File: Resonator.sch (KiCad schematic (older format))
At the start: 29 parts, among them J1 Conn_01x04_Male, SW1 Rotary_Encoder_Switch, SW2 SW_Push, U1 STM32H750VBTx, U2 AT25xxx, U3 IPS240x240, Y1 ABM8G-25.000MHZ-18-D2Y-T

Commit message: Re-annotation.
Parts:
- renumbered R4 to R1, R5 to R2, R6 to R3, R1 to R4, R7 to R5, R2 to R6, R3 to R7, SW2 to SW1, SW1 to SW2, U3 to U2, U2 to U3
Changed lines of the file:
@@
 $Descr A3 16535 11693
 encoding utf-8
-Sheet 1 6
+Sheet 1 11
 Title "Resonator"
 Date "2021-11-21"
@@
 Connection ~ 7650 2750
 $Comp
-L power:+3.3V #PWR013
+L power:+3.3V #PWR012
 U 1 1 61D958D9
 P 7650 2750
-F 0 "#PWR013" H 7650 2600 50  0001 C CNN
+F 0 "#PWR012" H 7650 2600 50  0001 C CNN
 F 1 "+3.3V" H 7665 2923 50  0000 C CNN
 F 2 "" H 7650 2750 50  0001 C CNN
@@
 $EndComp
 $Comp
-L power:+3.3VA #PWR016
+L power:+3.3VA #PWR015
 U 1 1 61D96DEA
 P 8150 2750
-F 0 "#PWR016" H 8150 2600 50  0001 C CNN
+F 0 "#PWR015" H 8150 2600 50  0001 C CNN
 F 1 "+3.3VA" H 8165 2923 50  0000 C CNN
 F 2 "" H 8150 2750 50  0001 C CNN
@@
 $EndComp
 $Comp
-L power:GND #PWR012
+L power:GND #PWR011
 U 1 1 61D9B5CB
 P 7550 8250
-F 0 "#PWR012" H 7550 8000 50  0001 C CNN
+F 0 "#PWR011" H 7550 8000 50  0001 C CNN
 F 1 "GND" H 7555 8077 50  0000 C CNN
 F 2 "" H 7550 8250 50  0001 C CNN
@@
 	6950 3550 6950 3450
 $Comp
-L power:GND #PWR010
+L power:GND #PWR09
 U 1 1 61DA19D2
 P 6050 3800
-F 0 "#PWR010" H 6050 3550 50  0001 C CNN
+F 0 "#PWR09" H 6050 3550 50  0001 C CNN
 F 1 "GND" H 6055 3627 50  0000 C CNN
 F 2 "" H 6050 3800 50  0001 C CNN
@@
 Connection ~ 6050 3800
 $Comp
-L power:+3V3 #PWR04
+L power:+3V3 #PWR03
 U 1 1 61DAD533
 P 4050 10300
-F 0 "#PWR04" H 4050 10150 50  0001 C CNN
+F 0 "#PWR03" H 4050 10150 50  0001 C CNN
 F 1 "+3V3" H 4065 10473 50  0000 C CNN
 F 2 "" H 4050 10300 50  0001 C CNN
@@
 	4050 10300 4200 10300
 $Comp
-L power:GND #PWR05
+L power:GND #PWR04
 U 1 1 61DAD53E
 P 4050 10600
-F 0 "#PWR05" H 4050 10350 50  0001 C CNN
+F 0 "#PWR04" H 4050 10350 50  0001 C CNN
 F 1 "GND" H 4055 10427 50  0000 C CNN
 F 2 "" H 4050 10600 50  0001 C CNN
@@
 $EndComp
 $Comp
-L Device:R R4
+L Device:R R1
 U 1 1 61DB7AD0
 P 5750 3050
-F 0 "R4" V 5543 3050 50  0000 C CNN
+F 0 "R1" V 5543 3050 50  0000 C CNN
 F 1 "UNPOPULATED" V 5634 3050 50  0000 C CNN
 F 2 "Resistor_SMD:R_0603_1608Metric" V 5680 3050 50  0001 C CNN
@@
 $EndComp
 $Comp
-L Switch:SW_Push SW2
+L Switch:SW_Push SW1
 U 1 1 61DBD527
 P 6750 3050
-F 0 "SW2" H 6750 3335 50  0000 C CNN
+F 0 "SW1" H 6750 3335 50  0000 C CNN
 F 1 "SW_Push" H 6750 3244 50  0000 C CNN
 F 2 "Button_Switch_THT:SW_PUSH_6mm" H 6750 3250 50  0001 C CNN
@@
 	6950 2600 6900 2600
 $Comp
-L power:GND #PWR011
+L power:GND #PWR010
 U 1 1 61DC8FB1
 P 6300 2750
-F 0 "#PWR011" H 6300 2500 50  0001 C CNN
+F 0 "#PWR010" H 6300 2500 50  0001 C CNN
 F 1 "GND" H 6305 2577 50  0000 C CNN
 F 2 "" H 6300 2750 50  0001 C CNN
@@
 	5700 4700 5700 4450
 $Comp
-L power:GND #PWR07
+L power:GND #PWR06
 U 1 1 61E01E16
 P 5700 5050
-F 0 "#PWR07" H 5700 4800 50  0001 C CNN
+F 0 "#PWR06" H 5700 4800 50  0001 C CNN
 F 1 "GND" H 5705 4877 50  0000 C CNN
 F 2 "" H 5700 5050 50  0001 C CNN
@@
 	7750 10300 7900 10300
 $Comp
-L power:GND #PWR015
+L power:GND #PWR014
 U 1 1 61E8662A
 P 7750 10600
-F 0 "#PWR015" H 7750 10350 50  0001 C CNN
+F 0 "#PWR014" H 7750 10350 50  0001 C CNN
 F 1 "GND" H 7755 10427 50  0000 C CNN
 F 2 "" H 7750 10600 50  0001 C CNN
@@
 	7750 10600 7900 10600
 $Comp
-L power:+3.3VA #PWR014
+L power:+3.3VA #PWR013
 U 1 1 61E8B8BA
 P 7750 10300
-F 0 "#PWR014" H 7750 10150 50  0001 C CNN
+F 0 "#PWR013" H 7750 10150 50  0001 C CNN
 F 1 "+3.3VA" H 7765 10473 50  0000 C CNN
 F 2 "" H 7750 10300 50  0001 C CNN
@@
 	7900 10600 8300 10600
 $Comp
-L Device:R R5
+L Device:R R2
 U 1 1 61ADEFE2
 P 5750 3450
-F 0 "R5" V 5543 3450 50  0000 C CNN
+F 0 "R2" V 5543 3450 50  0000 C CNN
 F 1 "10k" V 5634 3450 50  0000 C CNN
 F 2 "Resistor_SMD:R_0603_1608Metric" V 5680 3450 50  0001 C CNN
@@
 	6100 4800 6100 4950
 $Comp
-L Device:R R6
+L Device:R R3
 U 1 1 61AE0744
 P 6250 4950
-F 0 "R6" V 6043 4950 50  0000 C CNN
+F 0 "R3" V 6043 4950 50  0000 C CNN
 F 1 "470" V 6134 4950 50  0000 C CNN
 F 2 "Resistor_SMD:R_0603_1608Metric" V 6180 4950 50  0001 C CNN
@@
 	5750 3250 5750 3200
 $Comp
-L power:GND #PWR09
+L power:GND #PWR08
 U 1 1 61AF8BC1
 P 5750 3600
-F 0 "#PWR09" H 5750 3350 50  0001 C CNN
+F 0 "#PWR08" H 5750 3350 50  0001 C CNN
 F 1 "GND" H 5755 3427 50  0000 C CNN
 F 2 "" H 5750 3600 50  0001 C CNN
@@
 $EndComp
 $Comp
-L power:+3.3V #PWR08
+L power:+3.3V #PWR07
 U 1 1 61AF9828
 P 5750 2900
-F 0 "#PWR08" H 5750 2750 50  0001 C CNN
+F 0 "#PWR07" H 5750 2750 50  0001 C CNN
 F 1 "+3.3V" H 5765 3073 50  0000 C CNN
 F 2 "" H 5750 2900 50  0001 C CNN
@@
 P 13200 6950
 AR Path="/5DD41DD6/61DD28C6" Ref="U?"  Part="1"
-AR Path="/61DD28C6" Ref="U2"  Part="1"
+AR Path="/61DD28C6" Ref="U3"  Part="1"
 AR Path="/61DB1EC2/61DD28C6" Ref="U?"  Part="1"
-F 0 "U2" H 13200 7431 50  0000 C CNN
+F 0 "U3" H 13200 7431 50  0000 C CNN
 F 1 "AT25xxx" H 13200 7340 50  0000 C CNN
 F 2 "Package_SO:TSSOP-8_4.4x3mm_P0.65mm" H 13200 6950 50  0001 C CNN
@@
 P 13200 7350
 AR Path="/5DD41DD6/61DD28CC" Ref="#PWR?"  Part="1"
-AR Path="/61DD28CC" Ref="#PWR024"  Part="1"
+AR Path="/61DD28CC" Ref="#PWR018"  Part="1"
 AR Path="/61DB1EC2/61DD28CC" Ref="#PWR?"  Part="1"
-F 0 "#PWR024" H 13200 7100 50  0001 C CNN
+F 0 "#PWR018" H 13200 7100 50  0001 C CNN
 F 1 "GND" H 13205 7177 50  0000 C CNN
 F 2 "" H 13200 7350 50  0001 C CNN
@@
 P 13200 6400
 AR Path="/5DD41DD6/61DD28D3" Ref="#PWR?"  Part="1"
-AR Path="/61DD28D3" Ref="#PWR023"  Part="1"
+AR Path="/61DD28D3" Ref="#PWR017"  Part="1"
 AR Path="/61DB1EC2/61DD28D3" Ref="#PWR?"  Part="1"
-F 0 "#PWR023" H 13200 6250 50  0001 C CNN
+F 0 "#PWR017" H 13200 6250 50  0001 C CNN
 F 1 "+3.3V" H 13215 6573 50  0000 C CNN
 F 2 "" H 13200 6400 50  0001 C CNN
@@
 P 13300 3500
 AR Path="/5DD41DD6/61DE3E76" Ref="SW?"  Part="1"
-AR Path="/61DE3E76" Ref="SW1"  Part="1"
+AR Path="/61DE3E76" Ref="SW2"  Part="1"
 AR Path="/61DB1EC2/61DE3E76" Ref="SW?"  Part="1"
-F 0 "SW1" H 13300 3867 50  0000 C CNN
+F 0 "SW2" H 13300 3867 50  0000 C CNN
 F 1 "Rotary_Encoder_Switch" H 13300 3776 50  0000 C CNN
 F 2 "Rotary_Encoder:RotaryEncoder_Alps_EC11E-Switch_Vertical_H20mm" H 13150 3660 50  0001 C CNN
@@
 P 13300 3900
 AR Path="/5DD41DD6/61DE3E7C" Ref="#PWR?"  Part="1"
-AR Path="/61DE3E7C" Ref="#PWR03"  Part="1"
+AR Path="/61DE3E7C" Ref="#PWR019"  Part="1"
 AR Path="/61DB1EC2/61DE3E7C" Ref="#PWR?"  Part="1"
-F 0 "#PWR03" H 13300 3650 50  0001 C CNN
+F 0 "#PWR019" H 13300 3650 50  0001 C CNN
 F 1 "GND" H 13305 3727 50  0000 C CNN
 F 2 "" H 13300 3900 50  0001 C CNN
@@
 P 13750 3050
 AR Path="/61DB1EC2/61DE3E90" Ref="R?"  Part="1"
-AR Path="/61DE3E90" Ref="R3"  Part="1"
-F 0 "R3" H 13820 3096 50  0000 L CNN
+AR Path="/61DE3E90" Ref="R7"  Part="1"
+F 0 "R7" H 13820 3096 50  0000 L CNN
 F 1 "10k" H 13820 3005 50  0000 L CNN
 F 2 "Resistor_SMD:R_0603_1608Metric" V 13680 3050 50  0001 C CNN
@@
 P 12800 3050
 AR Path="/61DB1EC2/61DE3E96" Ref="R?"  Part="1"
-AR Path="/61DE3E96" Ref="R2"  Part="1"
-F 0 "R2" H 12870 3096 50  0000 L CNN
+AR Path="/61DE3E96" Ref="R6"  Part="1"
+F 0 "R6" H 12870 3096 50  0000 L CNN
 F 1 "10k" H 12870 3005 50  0000 L CNN
 F 2 "Resistor_SMD:R_0603_1608Metric" V 12730 3050 50  0001 C CNN
@@
 P 12500 3050
 AR Path="/61DB1EC2/61DE3E9C" Ref="R?"  Part="1"
-AR Path="/61DE3E9C" Ref="R1"  Part="1"
-F 0 "R1" H 12570 3096 50  0000 L CNN
+AR Path="/61DE3E9C" Ref="R4"  Part="1"
+F 0 "R4" H 12570 3096 50  0000 L CNN
 F 1 "10k" H 12570 3005 50  0000 L CNN
 F 2 "Resistor_SMD:R_0603_1608Metric" V 12430 3050 50  0001 C CNN
@@
 P 12500 2750
 AR Path="/61DB1EC2/61DE3EAB" Ref="#PWR?"  Part="1"
-AR Path="/61DE3EAB" Ref="#PWR01"  Part="1"
-F 0 "#PWR01" H 12500 2600 50  0001 C CNN
+AR Path="/61DE3EAB" Ref="#PWR016"  Part="1"
+F 0 "#PWR016" H 12500 2600 50  0001 C CNN
 F 1 "+3.3V" H 12515 2923 50  0000 C CNN
 F 2 "" H 12500 2750 50  0001 C CNN
@@
 P 5550 9350
 AR Path="/5DD41DD6/61DED307" Ref="#PWR?"  Part="1"
-AR Path="/61DED307" Ref="#PWR06"  Part="1"
+AR Path="/61DED307" Ref="#PWR05"  Part="1"
 AR Path="/61DB1EC2/61DED307" Ref="#PWR?"  Part="1"
-F 0 "#PWR06" H 5550 9100 50  0001 C CNN
+F 0 "#PWR05" H 5550 9100 50  0001 C CNN
 F 1 "GND" H 5555 9177 50  0000 C CNN
 F 2 "" H 5550 9350 50  0001 C CNN
@@
 P 12700 5250
 AR Path="/5DD41DD6/61E13169" Ref="R?"  Part="1"
-AR Path="/61E13169" Ref="R7"  Part="1"
+AR Path="/61E13169" Ref="R5"  Part="1"
 AR Path="/61DB1EC2/61E13169" Ref="R?"  Part="1"
-F 0 "R7" V 12493 5250 50  0000 C CNN
+F 0 "R5" V 12493 5250 50  0000 C CNN
 F 1 "1k" V 12584 5250 50  0000 C CNN
 F 2 "Resistor_SMD:R_0603_1608Metric" V 12630 5250 50  0001 C CNN
@@
 P 13300 5700
 AR Path="/5DD41DD6/61E13170" Ref="#PWR?"  Part="1"
-AR Path="/61E13170" Ref="#PWR026"  Part="1"
+AR Path="/61E13170" Ref="#PWR021"  Part="1"
 AR Path="/61DB1EC2/61E13170" Ref="#PWR?"  Part="1"
-F 0 "#PWR026" H 13300 5450 50  0001 C CNN
+F 0 "#PWR021" H 13300 5450 50  0001 C CNN
 F 1 "GND" H 13305 5527 50  0000 C CNN
 F 2 "" H 13300 5700 50  0001 C CNN
@@
 P 13300 4600
 AR Path="/5DD41DD6/61E13177" Ref="#PWR?"  Part="1"
-AR Path="/61E13177" Ref="#PWR025"  Part="1"
+AR Path="/61E13177" Ref="#PWR020"  Part="1"
 AR Path="/61DB1EC2/61E13177" Ref="#PWR?"  Part="1"
-F 0 "#PWR025" H 13300 4450 50  0001 C CNN
+F 0 "#PWR020" H 13300 4450 50  0001 C CNN
 F 1 "+3.3V" H 13315 4773 50  0000 C CNN
 F 2 "" H 13300 4600 50  0001 C CNN
@@
 TFT_RES
 $Comp
-L IPS240x240:IPS240x240 U3
+L IPS240x240:IPS240x240 U2
 U 1 1 61E39E11
 P 13150 4400
-F 0 "U3" H 13300 4131 50  0000 C CNN
+F 0 "U2" H 13300 4131 50  0000 C CNN
 F 1 "IPS240x240" H 13300 4040 50  0000 C CNN
 F 2 "" H 13150 4400 50  0001 C CNN
@@
 	2550 5950 2650 5950
 $Comp
-L power:GND #PWR02
+L power:GND #PWR01
 U 1 1 61E78173
 P 1750 6000
-F 0 "#PWR02" H 1750 5750 50  0001 C CNN
+F 0 "#PWR01" H 1750 5750 50  0001 C CNN
 F 1 "GND" H 1755 5827 50  0000 C CNN
 F 2 "" H 1750 6000 50  0001 C CNN
@@
 	2550 6400 2650 6400
 $Comp
-L power:GND #PWR?
+L power:GND #PWR02
 U 1 1 621F67D5
 P 1750 6450
-F 0 "#PWR?" H 1750 6200 50  0001 C CNN
+F 0 "#PWR02" H 1750 6200 50  0001 C CNN
 F 1 "GND" H 1755 6277 50  0000 C CNN
 F 2 "" H 1750 6450 50  0001 C CNN

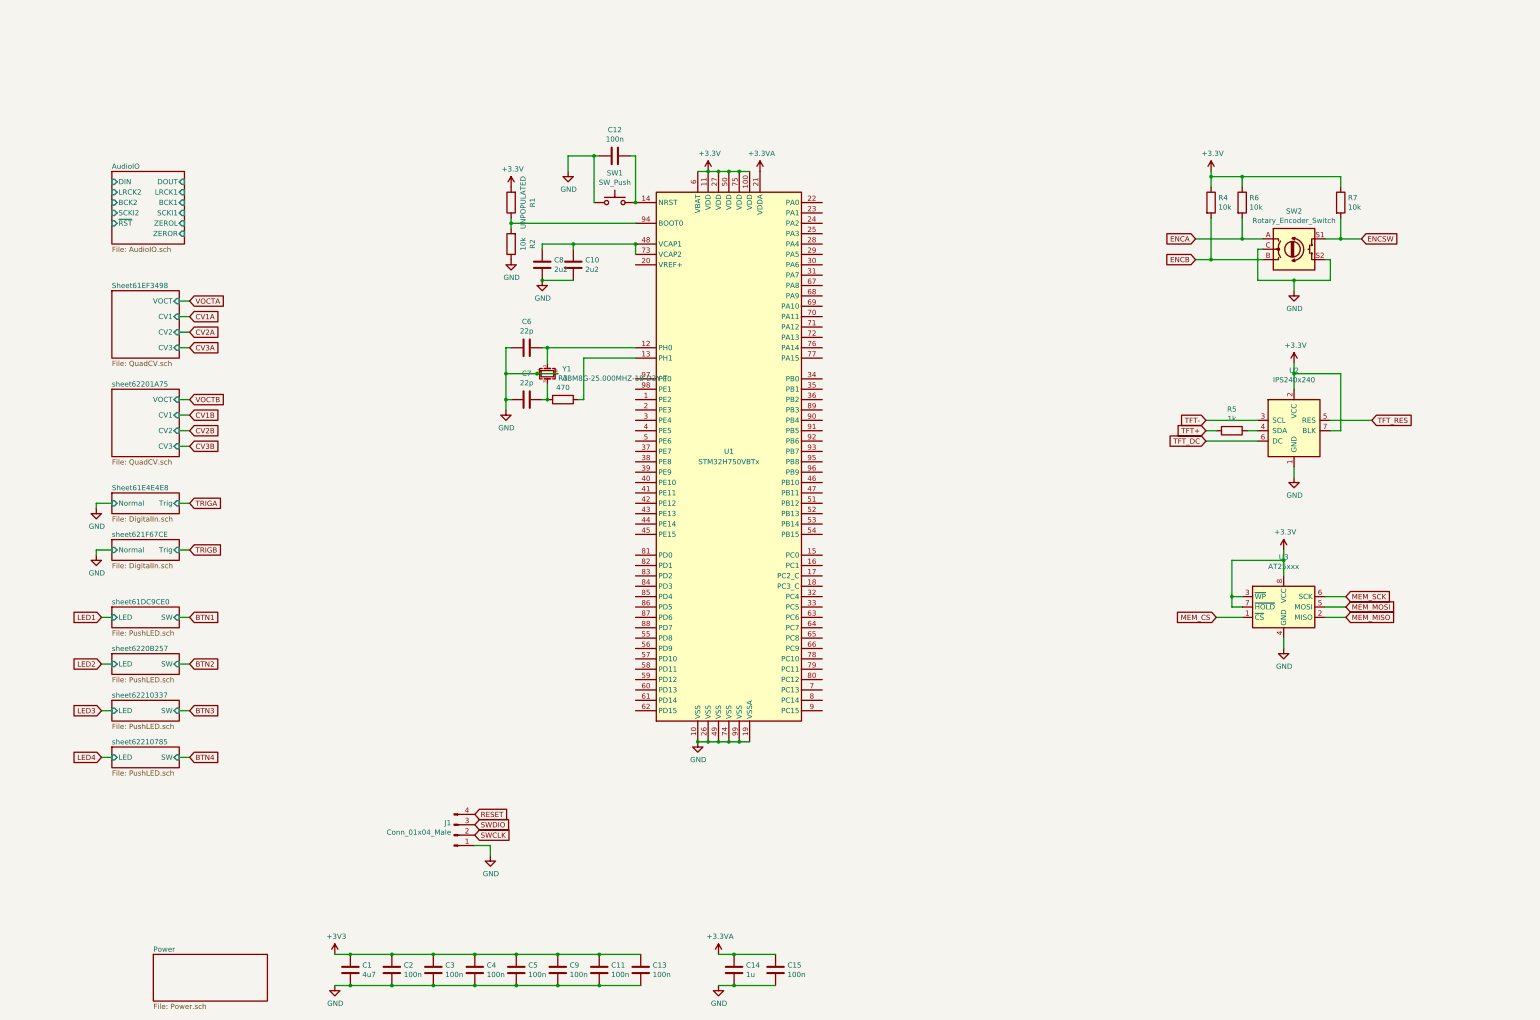
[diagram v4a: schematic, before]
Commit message: Assigned pins and cleared schema rules.
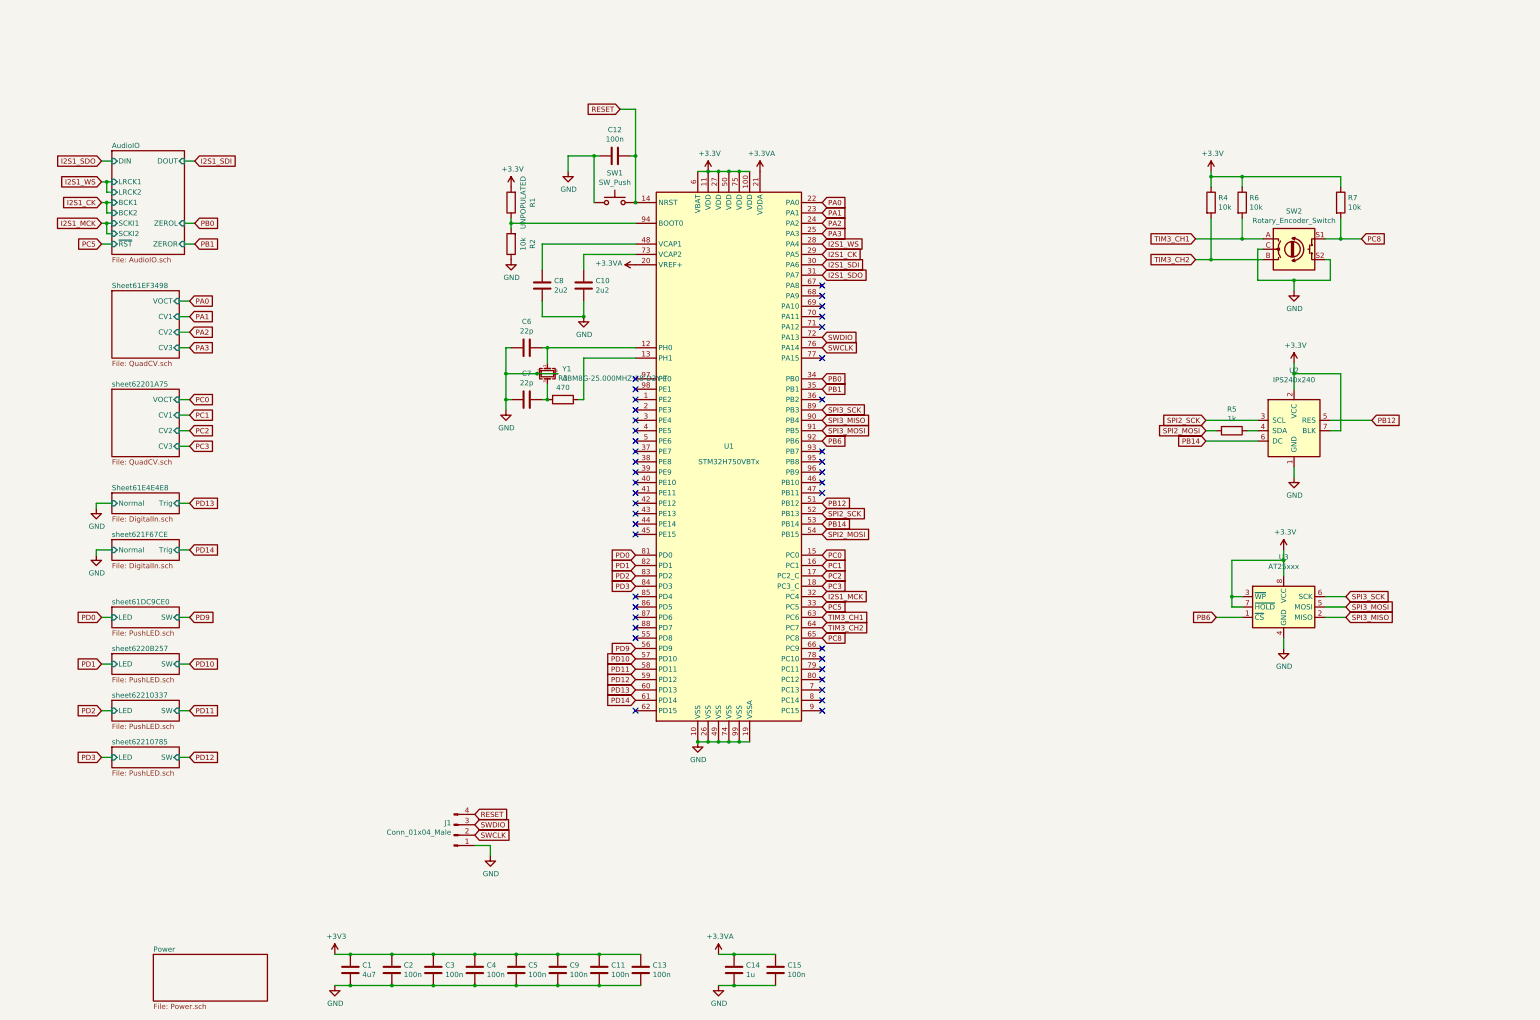
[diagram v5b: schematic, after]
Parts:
- U2: footprint (none) -> Local:IPS240x240
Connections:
- net ENCA is gone; now on net TIM3_CH1: R6.2, SW2.A
- net ENCB is gone; now on net TIM3_CH2: R4.2, SW2.B
- net ENCSW is gone; now on net PC8: R7.2, SW2.S1
- net MEM_CS is gone; now on net PB6: U3.1 (~CS)
- net MEM_MISO is gone; now on net SPI3_MISO: U3.2 (MISO)
- net MEM_MOSI is gone; now on net SPI3_MOSI: U3.5 (MOSI)
- net MEM_SCK is gone; now on net SPI3_SCK: U3.6 (SCK)
- net TFT+ is gone; now on net SPI2_MOSI: R5.2
- net TFT- is gone; now on net SPI2_SCK: U2.3 (SCL)
- net TFT_DC is gone; now on net PB14: U2.6 (DC)
- net TFT_RES is gone; now on net PB12: U2.5 (RES)
- net +3.3VA: now also U1.20 (VREF+)
- net RESET: now also C12.1, SW1.2, U1.14 (NRST)
- net SWCLK: now also U1.76 (PA14)
- net SWDIO: now also U1.72 (PA13)
- net PC0: now reaches U1.15 (PC0)
- net PC1: now reaches U1.16 (PC1)
- net PC2: now reaches U1.17 (PC2_C)
- net PC3: now reaches U1.18 (PC3_C)
- net PA0: now reaches U1.22 (PA0)
- net PA1: now reaches U1.23 (PA1)
- net PA2: now reaches U1.24 (PA2)
- net PA3: now reaches U1.25 (PA3)
- net I2S1_WS: now reaches U1.28 (PA4)
- net I2S1_CK: now reaches U1.29 (PA5)
- net I2S1_SDI: now reaches U1.30 (PA6)
- net I2S1_SDO: now reaches U1.31 (PA7)
- net I2S1_MCK: now reaches U1.32 (PC4)
- net PC5: now reaches U1.33 (PC5)
- net PB0: now reaches U1.34 (PB0)
- net PB1: now reaches U1.35 (PB1)
- net at C10.1, U1.73 (VCAP2): no longer C8.1, U1.48 (VCAP1)
- net PB12: now reaches U1.51 (PB12)
- net SPI2_SCK: now reaches U1.52 (PB13)
- net PB14: now reaches U1.53 (PB14)
- net SPI2_MOSI: now reaches U1.54 (PB15)
- net PD9: now reaches U1.56 (PD9)
- net PD10: now reaches U1.57 (PD10)
- net PD11: now reaches U1.58 (PD11)
- net PD12: now reaches U1.59 (PD12)
- net PD13: now reaches U1.60 (PD13)
- net PD14: now reaches U1.61 (PD14)
- net TIM3_CH1: now reaches U1.63 (PC6)
- net TIM3_CH2: now reaches U1.64 (PC7)
- net PC8: now reaches U1.65 (PC8)
- net PD0: now reaches U1.81 (PD0)
- net PD1: now reaches U1.82 (PD1)
- net PD2: now reaches U1.83 (PD2)
- net PD3: now reaches U1.84 (PD3)
- net SPI3_SCK: now reaches U1.89 (PB3)
- net SPI3_MISO: now reaches U1.90 (PB4)
- net SPI3_MOSI: now reaches U1.91 (PB5)
- net PB6: now reaches U1.92 (PB6)
- new net: C8.1, U1.48 (VCAP1)
- no-connect marks 0 -> 41
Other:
- moved on the sheet: C10, C8
